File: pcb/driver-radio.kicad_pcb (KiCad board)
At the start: 4 copper layers, 72 x 72 mm, 18 parts, among them J2 Conn_01x02_MountingPin, J3 Conn_01x02_MountingPin, U7 TCAN1042HGV

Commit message: Merging in work from FSAE repo from when I forgot this one existed
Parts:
- added C1: C, Capacitor_SMD:C_0402_1005Metric, F.Cu at (130.2, 89.2)
- added C10: 0.1u, Capacitor_SMD:C_0402_1005Metric, F.Cu at (151.5, 71.3)
- added C11: 4.7u, Capacitor_SMD:C_0805_2012Metric, F.Cu at (154.3, 65.5)
- added C12: 4.7u, Capacitor_SMD:C_0805_2012Metric, F.Cu at (152.5, 63.7)
- added C13: 47u, Capacitor_SMD:C_1206_3216Metric, F.Cu at (158.1, 48.2)
- added C14: 47u, Capacitor_SMD:C_1206_3216Metric, F.Cu at (158.1, 51.2)
- added C15: 1u, Capacitor_SMD:C_0402_1005Metric, F.Cu at (158.2, 53.8)
- added C17: 10u, Capacitor_SMD:C_0402_1005Metric, F.Cu at (150.8, 72.0)
- added C18: 4.7u, Capacitor_SMD:C_0402_1005Metric, F.Cu at (153.6, 75.7)
- added C2: 1.2n, Capacitor_SMD:C_0402_1005Metric, F.Cu at (123.9, 89.9)
- added C21: 0.1u, Capacitor_SMD:C_0402_1005Metric, F.Cu at (139.5, 54.4)
- added C22: 10u, Capacitor_SMD:C_0402_1005Metric, F.Cu at (137.5, 55.4)
- added C23: 1u, Capacitor_SMD:C_0402_1005Metric, F.Cu at (135.5, 57.4)
- added C24: 0.1u, Capacitor_SMD:C_0402_1005Metric, F.Cu at (139.5, 55.4)
- added C25: 10u, Capacitor_SMD:C_0402_1005Metric, F.Cu at (137.5, 56.4)
- added C26: 0.1u, Capacitor_SMD:C_0402_1005Metric, F.Cu at (139.5, 56.4)
- added C27: 10u, Capacitor_SMD:C_0402_1005Metric, F.Cu at (139.5, 57.4)
- added C3: 3300p, Capacitor_SMD:C_0402_1005Metric, F.Cu at (127.4, 87.8)
- added C4: 10u, Capacitor_SMD:C_0402_1005Metric, F.Cu at (142.0, 84.5)
- added C5: 1u, Capacitor_SMD:C_0402_1005Metric, F.Cu at (124.8, 91.8)
- added C8: 0.1u, Capacitor_SMD:C_0402_1005Metric, F.Cu at (151.6, 79.2)
- added C9: 10u, Capacitor_SMD:C_0402_1005Metric, F.Cu at (147.0, 66.3)
- added D1: LED, LED_SMD:LED_0402_1005Metric, F.Cu at (145.5, 34.0)
- added D2: LED, LED_SMD:LED_0402_1005Metric, F.Cu at (147.5, 34.0)
- added D3: LED, LED_SMD:LED_0402_1005Metric, F.Cu at (64.5, 104.0)
- added D4: LED, LED_SMD:LED_0402_1005Metric, F.Cu at (64.5, 106.0)
- added D5: LED, LED_SMD:LED_0402_1005Metric, F.Cu at (64.5, 108.0)
- added D6: LED, LED_SMD:LED_0402_1005Metric, F.Cu at (64.5, 110.0)
- added D8: LED, Diode_SMD:D_0402_1005Metric, F.Cu at (116.0, 84.5)
- added FL1: LFCN-530, Filter:Filter_Mini-Circuits_FV1206, F.Cu at (166.4, 42.9)
- added J1: Conn_01x05_Pin, Connector_PinHeader_2.54mm:PinHeader_1x05_P2.54mm_Vertical, F.Cu at (116.5, 67.0)
- added J5: Micro_SD_Card_Det_Hirose_DM3AT, Connector_Card:microSD_HC_Hirose_DM3BT-DSF-PEJS, F.Cu at (141.6, 95.0)
- added J6: Conn_Coaxial, Connector_Coaxial:SMA_Molex_73251-1153_EdgeMount_Horizontal, F.Cu at (166.5, 36.8)
- added JP1: SolderJumper_2_Open, Jumper:SolderJumper-2_P1.3mm_Open_RoundedPad1.0x1.5mm, F.Cu at (120.0, 89.6)
- added R1: 18k, Resistor_SMD:R_0402_1005Metric, F.Cu at (128.4, 94.5)
- added R14: 10k, Resistor_SMD:R_0402_1005Metric, F.Cu at (137.5, 57.4)
- added R15: 33, Resistor_SMD:R_0402_1005Metric, F.Cu at (124.1, 79.5)
- added R16: 1.6k, Resistor_SMD:R_0402_1005Metric, F.Cu at (124.9, 88.8)
- added R17: ~, Resistor_SMD:R_0402_1005Metric, F.Cu at (129.5, 89.9)
- added R18: R, Resistor_SMD:R_0402_1005Metric, F.Cu at (130.9, 91.3)
- added R19: 500, Resistor_SMD:R_0402_1005Metric, F.Cu at (118.0, 84.5)
- added R2: 55k, Resistor_SMD:R_0402_1005Metric, F.Cu at (129.5, 92.7)
- added R20: 91k, Resistor_SMD:R_0402_1005Metric, F.Cu at (127.0, 93.8)
- added R21: 10k, Resistor_SMD:R_0402_1005Metric_Pad0.72x0.64mm_HandSolder, F.Cu at (146.0, 85.5)
- added R22: 10k, Resistor_SMD:R_0402_1005Metric_Pad0.72x0.64mm_HandSolder, F.Cu at (146.0, 84.0)
- added R23: 10k, Resistor_SMD:R_0402_1005Metric_Pad0.72x0.64mm_HandSolder, F.Cu at (146.0, 82.5)
- added R3: BOOK, Resistor_SMD:R_0402_1005Metric, F.Cu at (151.5, 62.4)
- added R4: 4.7k, Resistor_SMD:R_0402_1005Metric, F.Cu at (138.9, 79.0)
- added R5: 4.7k, Resistor_SMD:R_0402_1005Metric, F.Cu at (137.7, 79.0)
- added R6: BOOK, Resistor_SMD:R_0402_1005Metric, F.Cu at (155.3, 66.6)
- added R7: BOOK, Resistor_SMD:R_0402_1005Metric, F.Cu at (158.1, 55.7)
- added R8: 2.2k, Resistor_SMD:R_0402_1005Metric, F.Cu at (145.5, 37.1)
- added R9: 2.2k, Resistor_SMD:R_0402_1005Metric, F.Cu at (147.5, 37.1)
- added REF**: Smolhaj_Scale_0.1, Symbol:Smolhaj_Scale_0.1, F.Cu at (183.0, 50.5)
- added TP1: CAN_TX, 0_tp-ev24-nobacksilk:tp-ev24-nobacksilk, F.Cu at (129.5, 53.5)
- added TP10: A_OUT, 0_tp-ev24-nobacksilk:tp-ev24-nobacksilk, F.Cu at (151.8, 68.0)
- added TP11: A_IN, 0_tp-ev24-nobacksilk:tp-ev24-nobacksilk, F.Cu at (150.0, 66.2)
- added TP12: SD0, 0_tp-ev24-nobacksilk:tp-ev24-nobacksilk, F.Cu at (119.0, 74.5)
- added TP16: SDCLK, 0_tp-ev24-nobacksilk:tp-ev24-nobacksilk, F.Cu at (124.5, 56.5)
- added TP17: SDCMD, 0_tp-ev24-nobacksilk:tp-ev24-nobacksilk, F.Cu at (119.0, 71.5)
- added TP2: CAN_RX, 0_tp-ev24-nobacksilk:tp-ev24-nobacksilk, F.Cu at (135.5, 53.5)
- added TP3: I2C_CTRL, 0_tp-ev24-nobacksilk:tp-ev24-nobacksilk, F.Cu at (136.1, 81.8)
- added TP4: I2C_CLK, 0_tp-ev24-nobacksilk:tp-ev24-nobacksilk, F.Cu at (142.0, 79.3)
- added TP5: MCLK, 0_tp-ev24-nobacksilk:tp-ev24-nobacksilk, F.Cu at (157.7, 106.8)
- added TP6: LRC, 0_tp-ev24-nobacksilk:tp-ev24-nobacksilk, F.Cu at (154.8, 109.0)
- added TP7: BCLK, 0_tp-ev24-nobacksilk:tp-ev24-nobacksilk, F.Cu at (153.4, 111.8)
- added TP8: SDIN, 0_tp-ev24-nobacksilk:tp-ev24-nobacksilk, F.Cu at (153.8, 115.0)
- added TP9: SDOUT, 0_tp-ev24-nobacksilk:tp-ev24-nobacksilk, F.Cu at (156.3, 118.2)
- added U1: TPS259474ARPWR, 0_tps259474arpwr:IC_TPS259474ARPWR, F.Cu at (127.2, 90.7)
- added U2: ESP32-WROOM-32U, RF_Module:ESP32-WROOM-32U, F.Cu at (131.2, 68.1)
- added U3: TLV70220PDBVR, Package_TO_SOT_SMD:SOT-23-5, F.Cu at (154.0, 78.5)
- added U4: SA868, 0_SA868:sa868, F.Cu at (170.6, 68.7)
- added U5: SGTL5000XNLA3, Package_DFN_QFN:QFN-20-1EP_3x3mm_P0.4mm_EP1.65x1.65mm, F.Cu at (148.4, 69.6)
- moved C20 5.80 mm to (128.5, 48.5), turned to 90 degrees
- renumbered C20 to C19, C21 to C20, J2 to J3, J3 to J4, R18 to R10, R19 to R11, R20 to R12, R21 to R13, U7 to U6
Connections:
- net /CANH renamed /CAN Transciever/CANH
- net /CANL renamed /CAN Transciever/CANL
- net /CAR_HEARTBEAT renamed /MCU/WARNING
- H3 pad 1: +3V3 -> +3V3_UNFUSED
- R10 pad 2: Net-(D3-A) -> Net-(D5-A)
- R11 pad 1: /MAIN_LOOP -> /MCU/MAIN_LOOP
- R12 pad 1: /WARNING -> /MCU/CAR_HEARTBEAT
- R12 pad 2: Net-(D5-A) -> Net-(D3-A)
- R13 pad 1: /FAULT -> /MCU/FAULT
- U6 pad 1: /CAN_TX -> /CAN Transciever/CAN_TX
- U6 pad 4: /CAN_RX -> /CAN Transciever/CAN_RX
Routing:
- net +5V: track 0.00 -> 138.4 mm, vias 0 -> 1
- net +3V3: track 0.00 -> 34.6 mm
- net /MCU/ESP32_RX: track 0.00 -> 29.8 mm, vias 0 -> 1
- net /MCU/ESP32_TX: track 0.00 -> 27.7 mm, vias 0 -> 1
- net /MCU/~{RESET}: track 0.00 -> 26.3 mm, vias 0 -> 2
- net /Codec/I2S_BCLK: track 0.00 -> 22.0 mm
- net Net-(FL1-IN): track 0.00 -> 22.0 mm
- net /Codec/I2S_LRC: track 0.00 -> 21.1 mm
- net /Codec/I2S_SDOUT: track 0.00 -> 19.6 mm
- net /Codec/I2C_SDA: track 0.00 -> 19.4 mm
- net /Codec/I2C_CLK: track 0.00 -> 17.9 mm
- net /MCU/BOOT_SELECT: track 0.00 -> 17.2 mm
- net /Codec/I2S_SDIN: track 0.00 -> 16.6 mm
- net /CAN Transciever/CAN_RX: track 0.00 -> 14.9 mm
- net /CAN Transciever/CAN_TX: track 0.00 -> 10.9 mm
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
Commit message: Quite a few changes
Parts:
- removed the D3 at (64.5, 104.0)
- removed the D4 at (64.5, 106.0)
- removed the D5 at (64.5, 108.0)
- removed the D6 at (64.5, 110.0)
- removed REF**: Smolhaj_Scale_0.1, Symbol:Smolhaj_Scale_0.1
- added C6: 47u, Capacitor_SMD:C_1206_3216Metric, F.Cu at (158.1, 47.6)
- moved J1 63.2 mm to (171.0, 99.0), turned to -90 degrees
- moved TP16 45.9 mm to (130.5, 102.0), turned to 90 degrees
- moved R15 37.3 mm to (155.0, 100.5), turned to 90 degrees
- moved C21 35.2 mm to (130.9, 88.5), turned to -45 degrees
- moved TP6 32.4 mm to (138.5, 81.0)
- moved C22 31.8 mm to (131.4, 86.5), turned to -90 degrees
- moved TP7 31.7 mm to (146.0, 81.0)
- moved C23 31.2 mm to (133.4, 88.5), turned to 90 degrees
- moved C25 30.6 mm to (132.4, 86.5), turned to -90 degrees
- moved C24 30.3 mm to (131.4, 84.5), turned to 90 degrees
- moved J5 30.1 mm to (124.4, 70.4), turned to -90 degrees
- moved R14 29.4 mm to (133.4, 86.5), turned to 90 degrees
- moved C26 29.0 mm to (132.4, 84.5), turned to 90 degrees
- moved C27 27.8 mm to (133.4, 84.5), turned to 90 degrees
- moved U2 27.8 mm to (144.1, 92.8), turned to 0 degrees
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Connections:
- R10 pad 1: /MCU/WARNING -> /MCU/CAR_HEARTBEAT
- R10 pad 2: Net-(D5-A) -> Net-(D3-A)
- R12 pad 1: /MCU/CAR_HEARTBEAT -> /MCU/WARNING
- R12 pad 2: Net-(D3-A) -> Net-(D5-A)
- U2 pad 10: unconnected-(U2-IO25-Pad10) -> /MCU/MAIN_LOOP
- U2 pad 14: /MCU/FAULT -> /MCU/CAR_HEARTBEAT
- U2 pad 26: /MCU/MAIN_LOOP -> /MCU/PTT
- U2 pad 29: /MCU/CAR_HEARTBEAT -> /MCU/IS_RADIO_RECIEVING
- U2 pad 30: unconnected-(U2-IO18-Pad30) -> /MCU/FAULT
- U2 pad 7: /MCU/RADIO_STATUS -> /MCU/WARNING
- U4 pad 1: /MCU/RADIO_STATUS -> /MCU/IS_RADIO_RECIEVING
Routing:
- net +3V3: track 34.6 -> 151.0 mm, vias 0 -> 2
- net /MCU/RADIO ON/OFF: track 0.00 -> 106.7 mm
- net /MCU/PTT: track 0.00 -> 89.6 mm
- net /MCU/SD_DATA0: track 3.25 -> 87.5 mm
- net /MCU/SD_CMD: track 3.33 -> 82.6 mm, vias 0 -> 2
- net /MCU/MAIN_LOOP: track 0.00 -> 77.8 mm, vias 0 -> 2
- net /MCU/CAR_HEARTBEAT: track 0.00 -> 74.7 mm, vias 0 -> 2
- net /MCU/SD_CLK: track 0.00 -> 66.2 mm, vias 0 -> 2
- net /MCU/FAULT: track 0.00 -> 62.9 mm, vias 0 -> 2
- net /MCU/WARNING: track 0.00 -> 58.2 mm, vias 0 -> 2
- net /CAN Transciever/CAN_TX: track 10.9 -> 55.2 mm, vias 0 -> 1
- net /MCU/RF_TX: track 0.00 -> 38.8 mm, vias 0 -> 2
- net /CAN Transciever/CAN_RX: track 14.9 -> 52.6 mm, vias 0 -> 1
- net /MCU/RF_RX: track 0.00 -> 36.3 mm, vias 0 -> 2
- net /Codec/I2S_MCLK: track 0.00 -> 31.7 mm, vias 0 -> 2
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- added copper zone on F.Cu, net +3V3
- added copper zone on F.Cu, net +3V3_UNFUSED

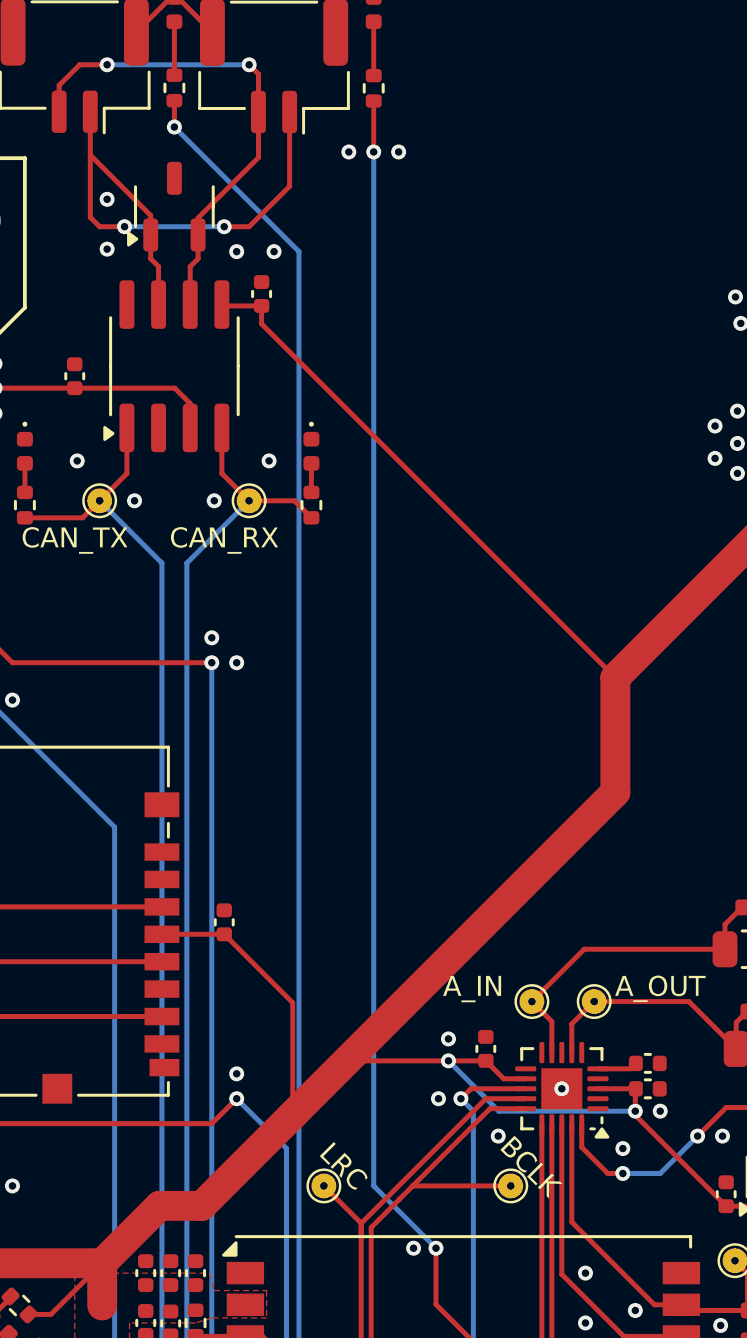
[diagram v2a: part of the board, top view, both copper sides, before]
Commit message: Removed baofeng outline
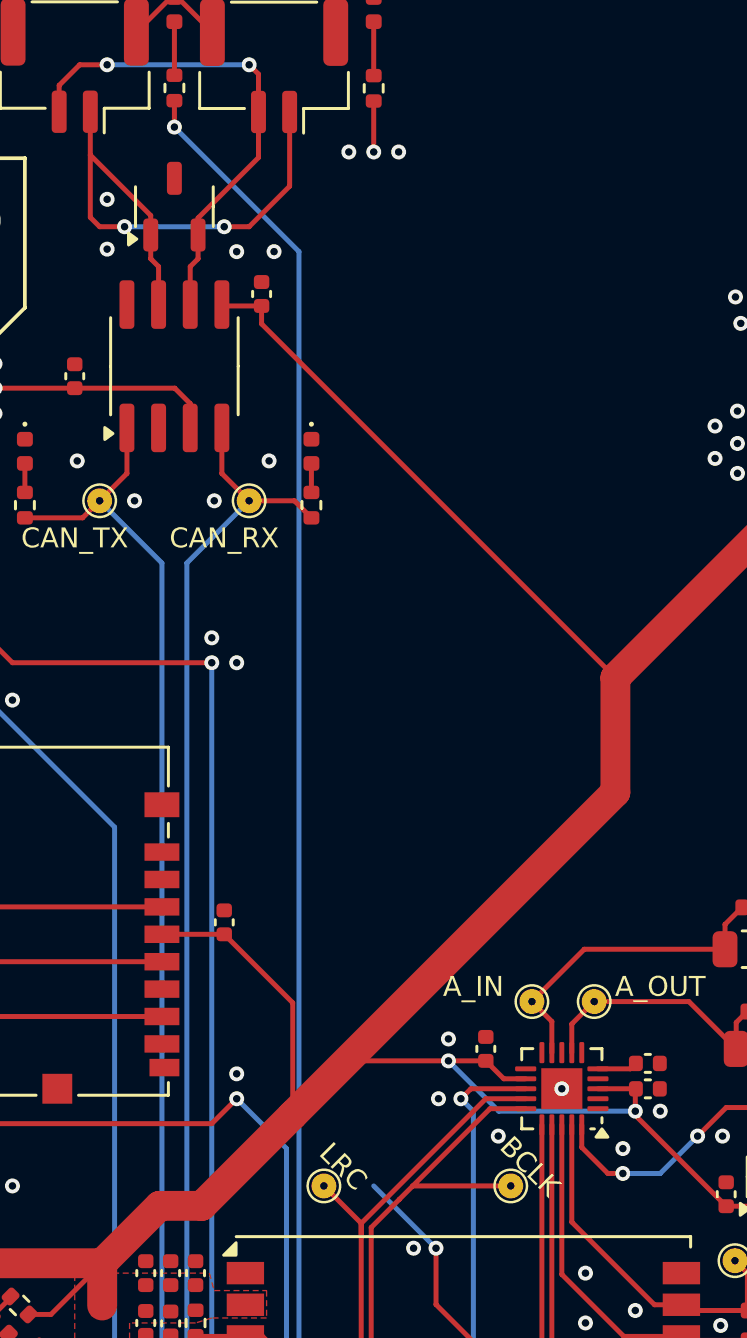
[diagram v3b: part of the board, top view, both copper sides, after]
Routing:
- net /MCU/FAULT: track 62.9 -> 21.4 mm
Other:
- board text removed: "MIC hole"
- board text removed: "PTT hole"
- board text removed: "Power hole"
- board text removed: "Speaker hole"

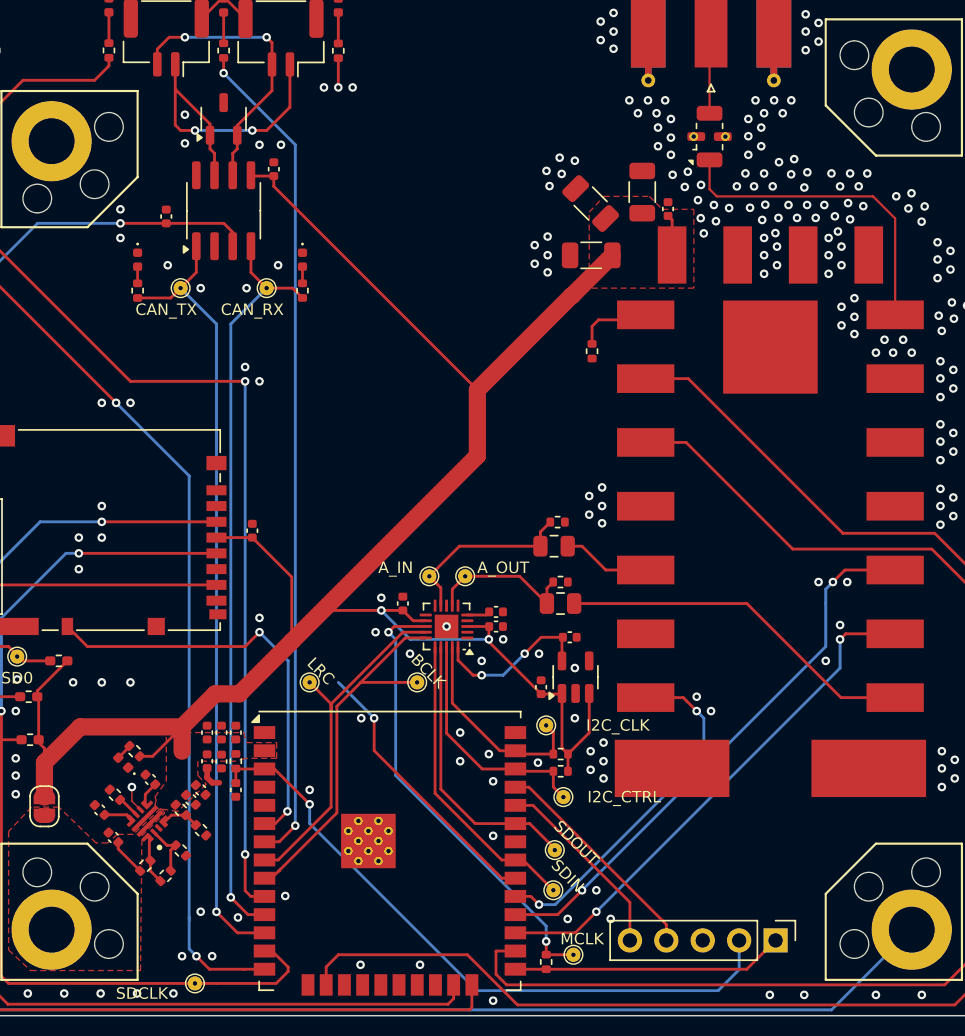
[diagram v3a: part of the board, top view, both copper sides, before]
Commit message: updated footprints
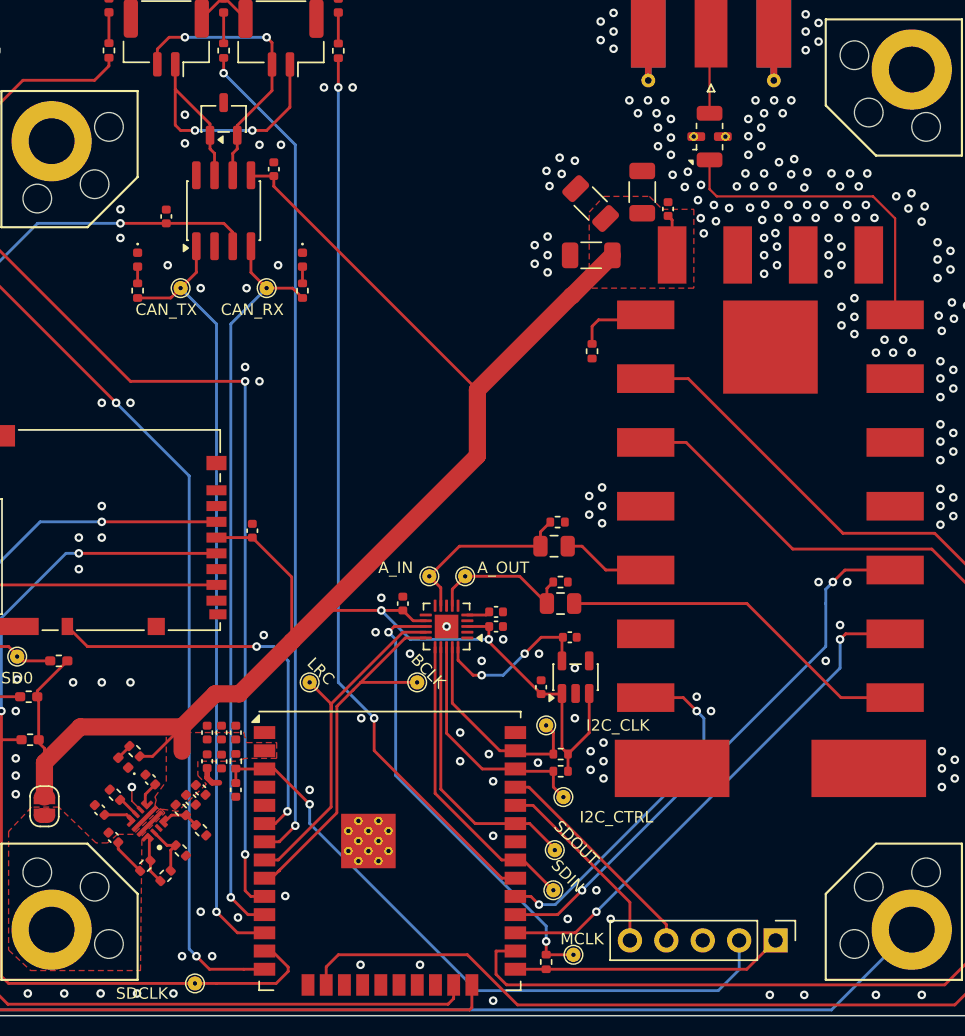
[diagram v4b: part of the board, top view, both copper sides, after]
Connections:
- net /MCU/RF_RX renamed /MCU/ESP32_RF_RX
- net /MCU/RF_TX renamed /MCU/ESP32_RF_TX
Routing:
- net /MCU/FAULT: track 21.4 -> 62.9 mm
- net /MCU/SD_DETECT: track 29.7 -> 28.9 mm

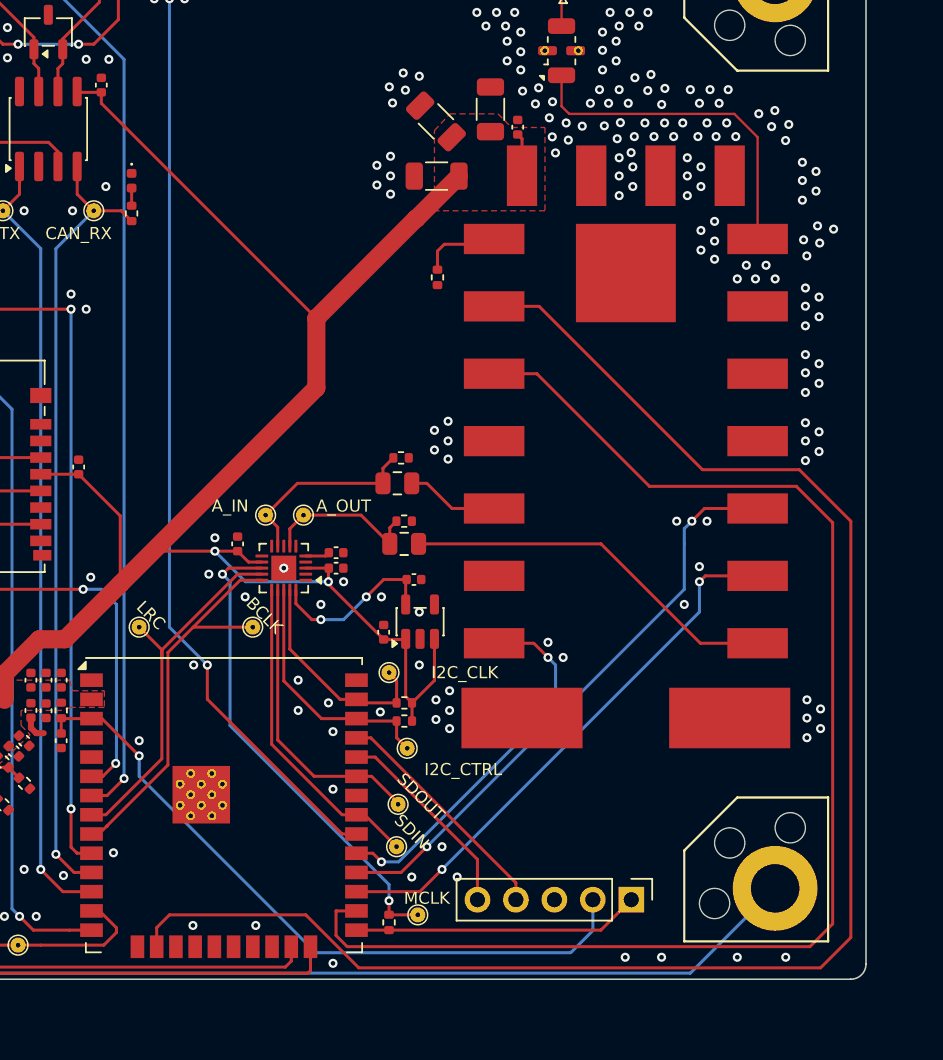
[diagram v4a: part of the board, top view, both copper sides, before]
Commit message: added 3d model
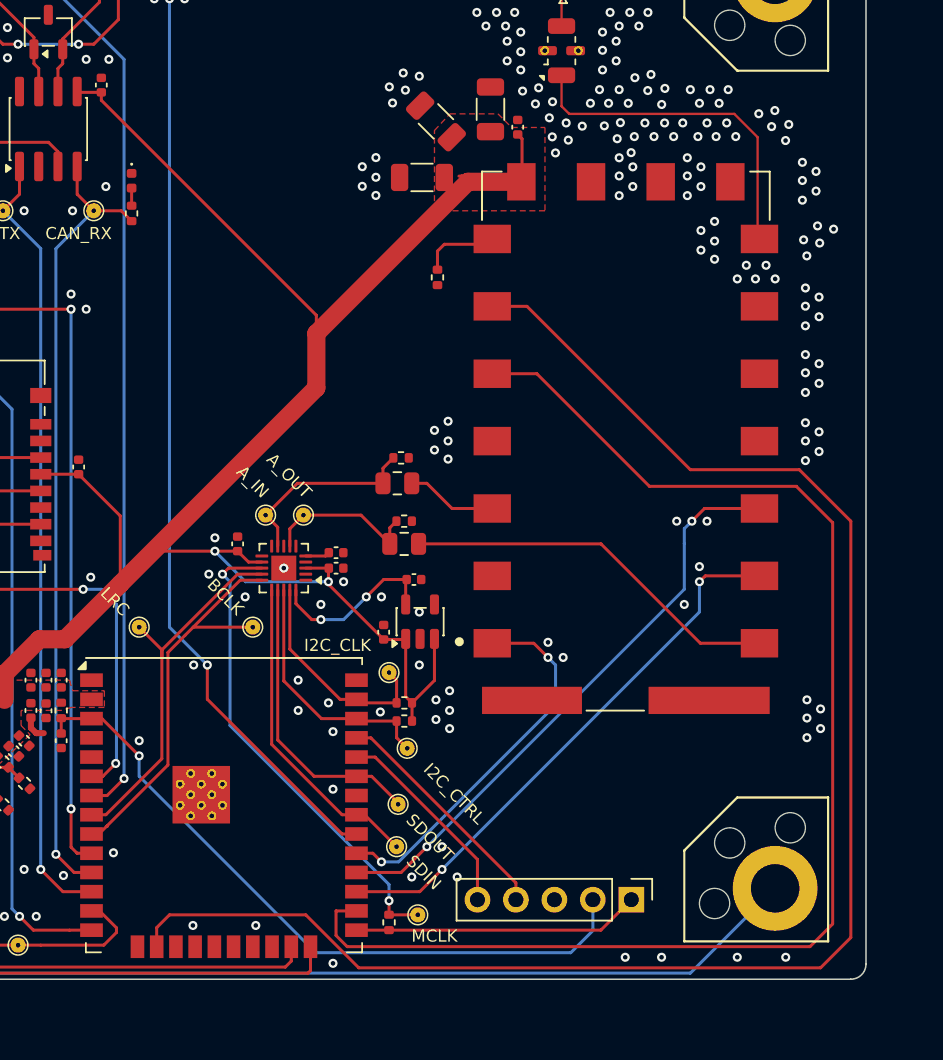
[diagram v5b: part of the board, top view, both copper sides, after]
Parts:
- U4: footprint 0_SA868:sa868 -> VHF_UHF_Modules:VHF_UHF_Module_generic
- moved C14 0.97 mm to (157.2, 51.3)
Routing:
- net +3V3: track 151.0 -> 155.4 mm
